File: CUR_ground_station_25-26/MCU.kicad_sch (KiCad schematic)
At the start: 1 part, among them U1 ESP32-S3-WROOM-1

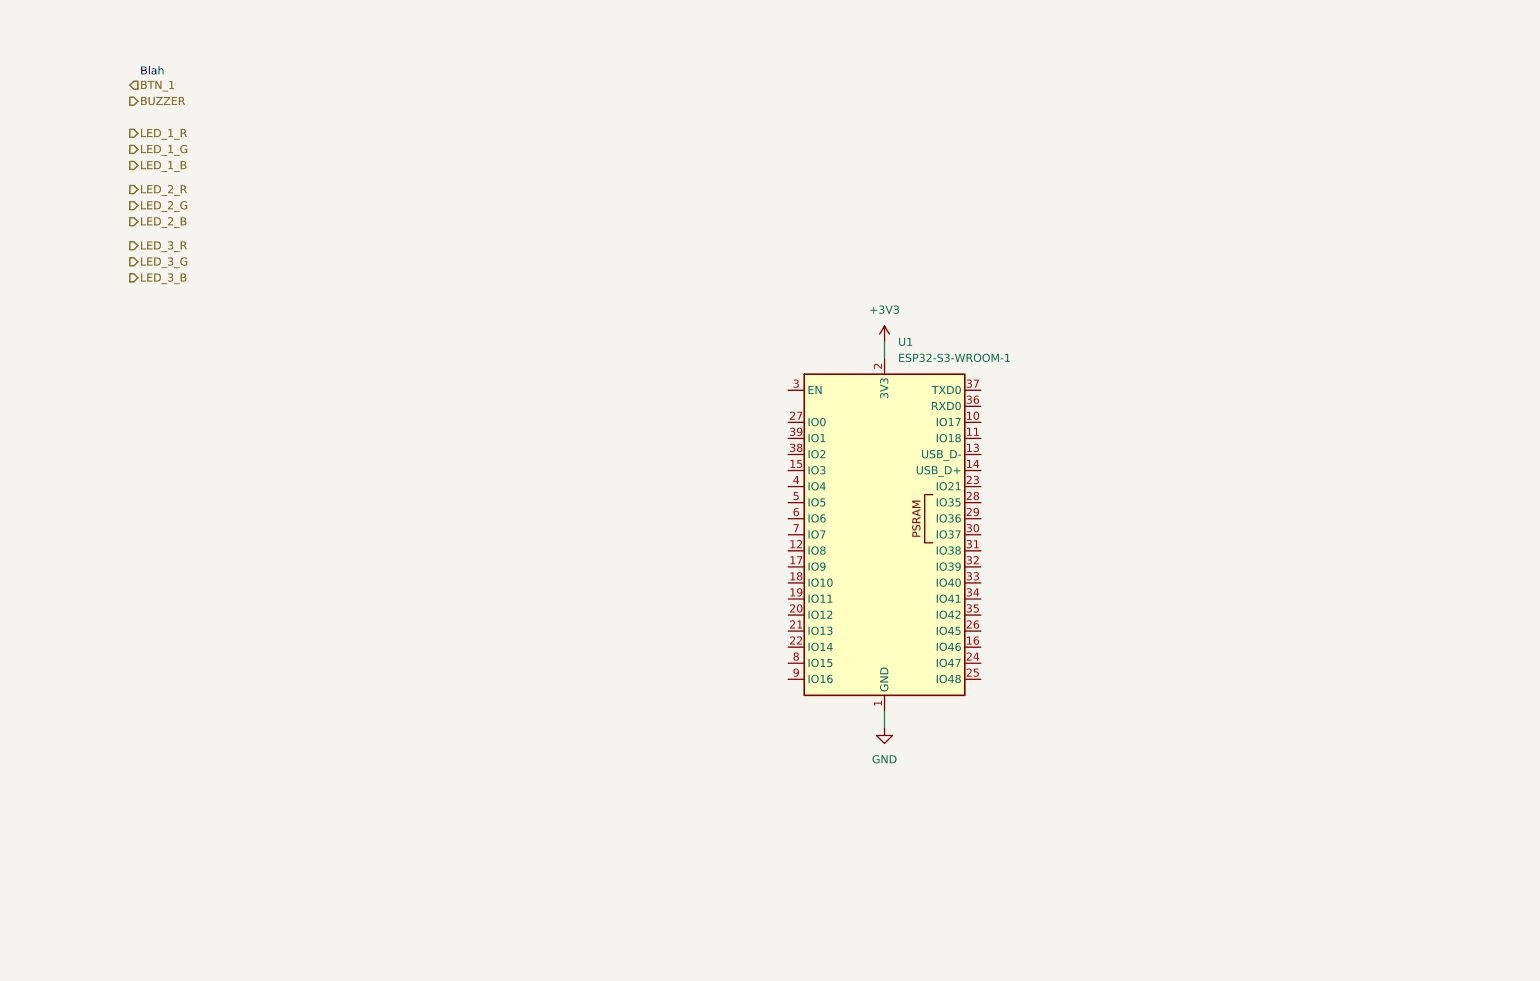
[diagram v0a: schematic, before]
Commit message: Add some required MCU components
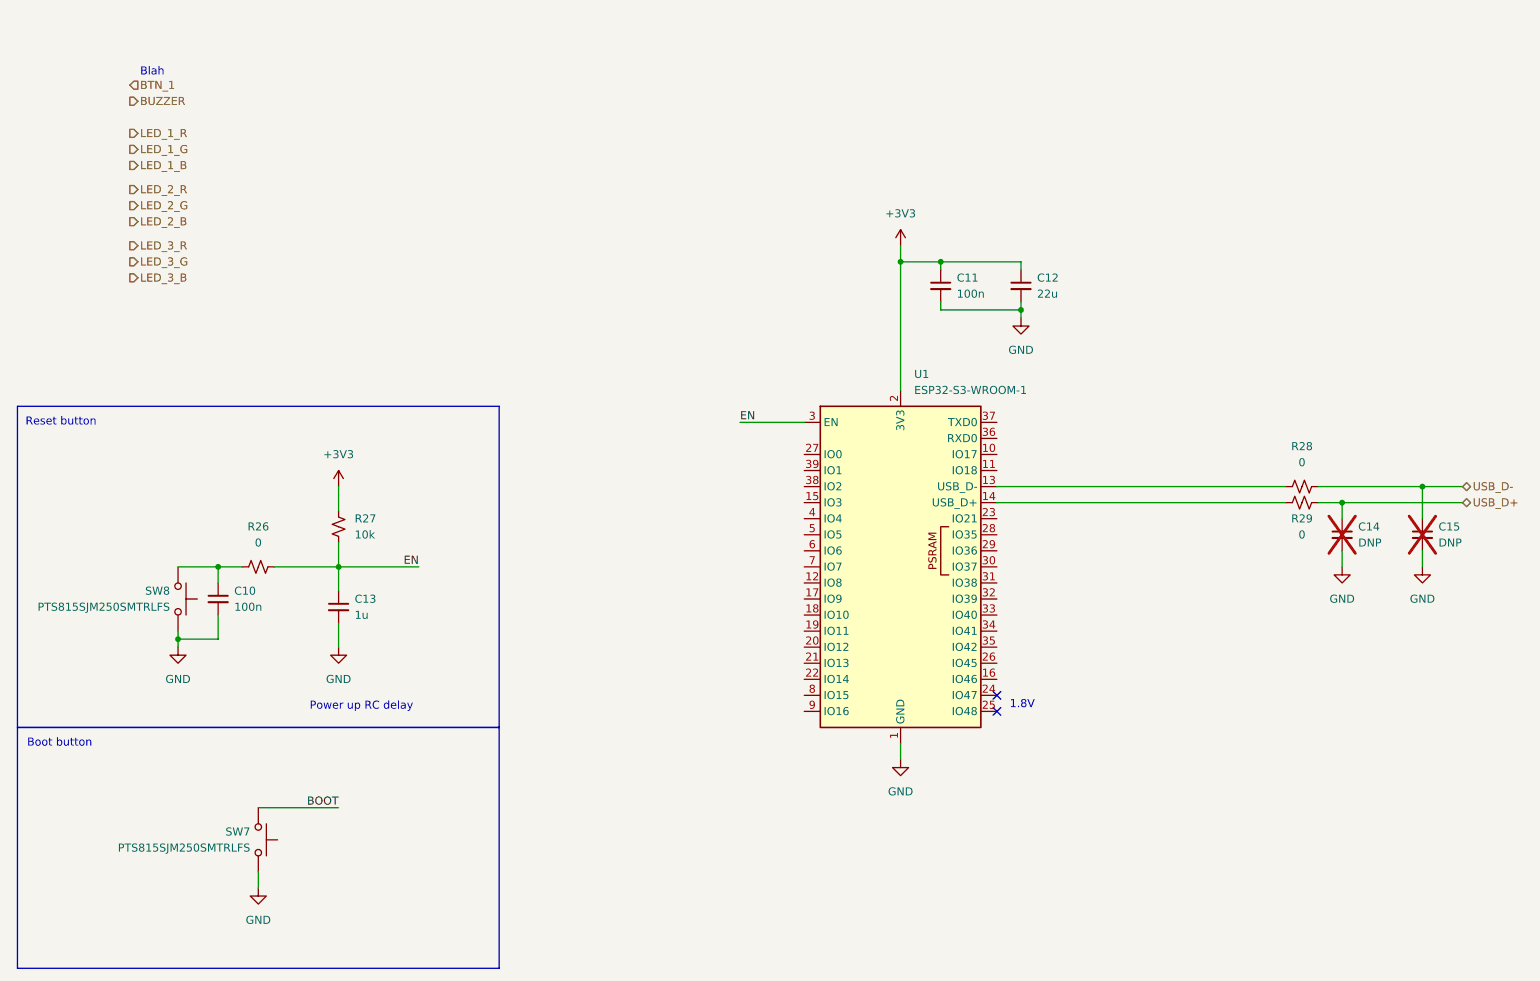
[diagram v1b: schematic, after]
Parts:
- added C10, C11: 100n, symbol Device:C_Small
- added C12: 22u, symbol Device:C_Small
- added C13: 1u, symbol Device:C_Small
- added C14, C15: DNP, symbol Device:C_Small
- added R26, R28, R29: 0, symbol Device:R_Small_US
- added R27: 10k, symbol Device:R_Small_US
- added SW7, SW8: PTS815SJM250SMTRLFS, symbol Switch:SW_Push
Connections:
- net +3V3: now also C11.1, C12.1, R27.1
- net GND: now also C10.2, C11.2, C12.2, C13.2, C14.2, C15.2, SW7.1, SW8.1
- net at U1.13 (USB_D-): now also R28.1
- net at U1.14 (USB_D+): now also R29.1
- net EN: now reaches U1.3 (EN)
- net EN: now also C13.1, R26.1, R27.2
- new net: C10.1, R26.2, SW8.2
- new net BOOT: SW7.2
- new net USB_D+: C14.1, R29.2
- new net USB_D-: C15.1, R28.2
- no-connect marks 0 -> 2
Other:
- note added: "1.8V"
- note added: "Boot button"
- note added: "Power up RC delay"
- note added: "Reset button"
- moved on the sheet: U1

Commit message: Sync sheet pins
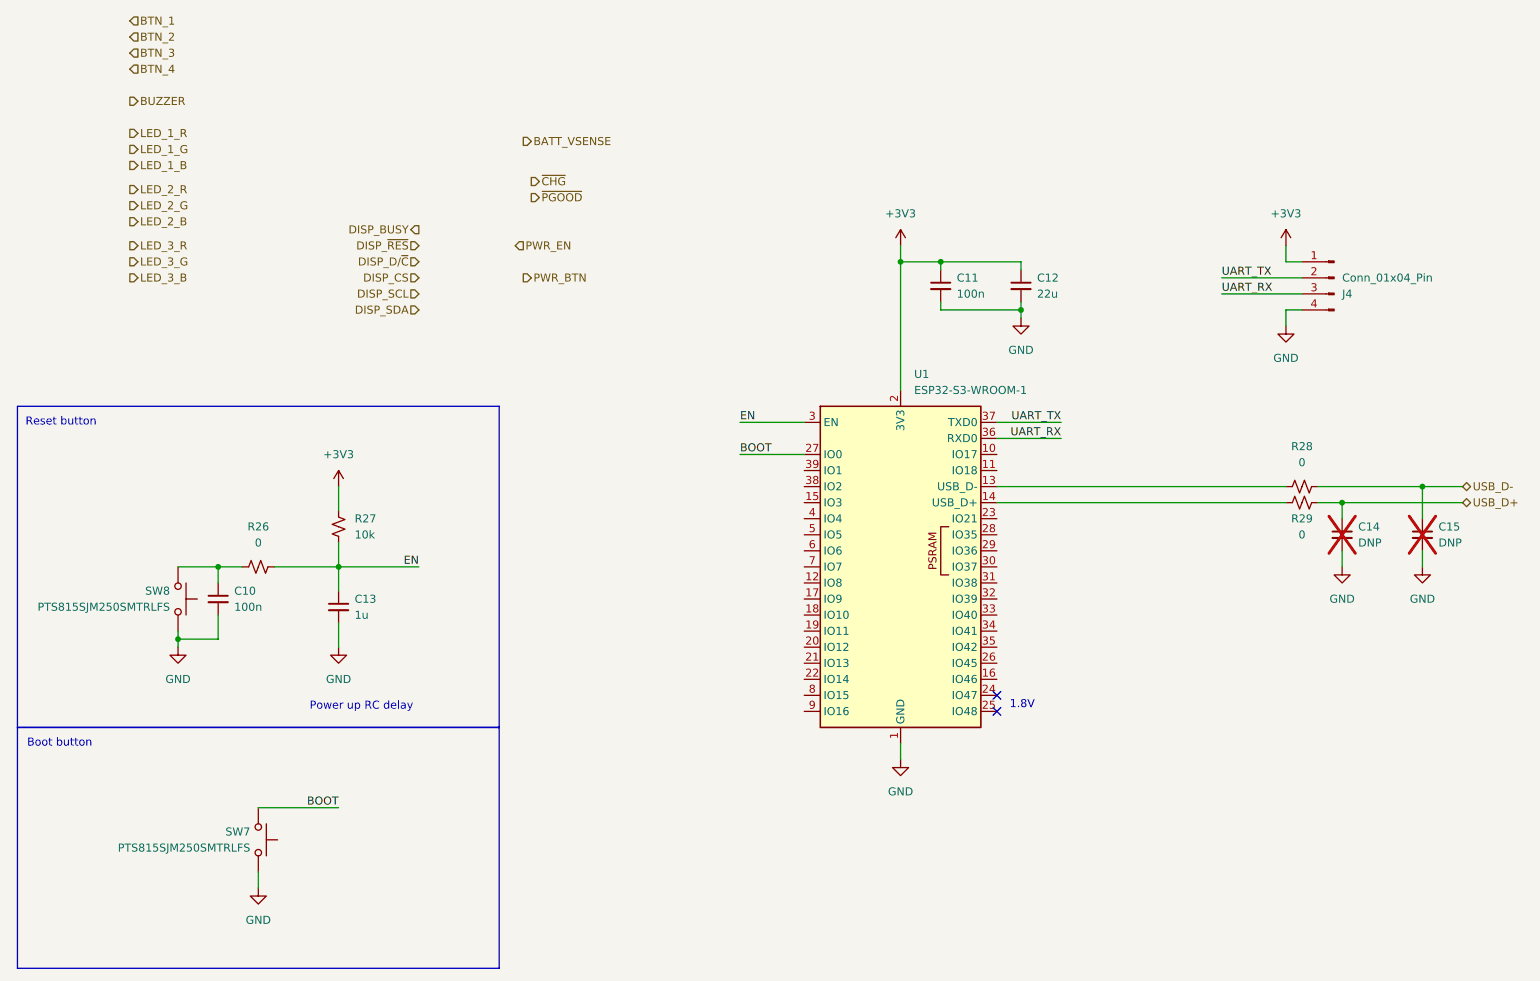
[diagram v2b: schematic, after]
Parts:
- added J4: Conn_01x04_Pin, symbol Connector:Conn_01x04_Pin
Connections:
- net +3V3: now also J4.1 (Pin_1)
- net BOOT: now also U1.27 (IO0)
- net GND: now also J4.4 (Pin_4)
- net UART_RX: now reaches U1.36 (RXD0)
- net UART_RX: now also J4.3 (Pin_3)
- net UART_TX: now reaches U1.37 (TXD0)
- net UART_TX: now also J4.2 (Pin_2)
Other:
- note removed: "Blah"

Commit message: Started placing pins on MCU
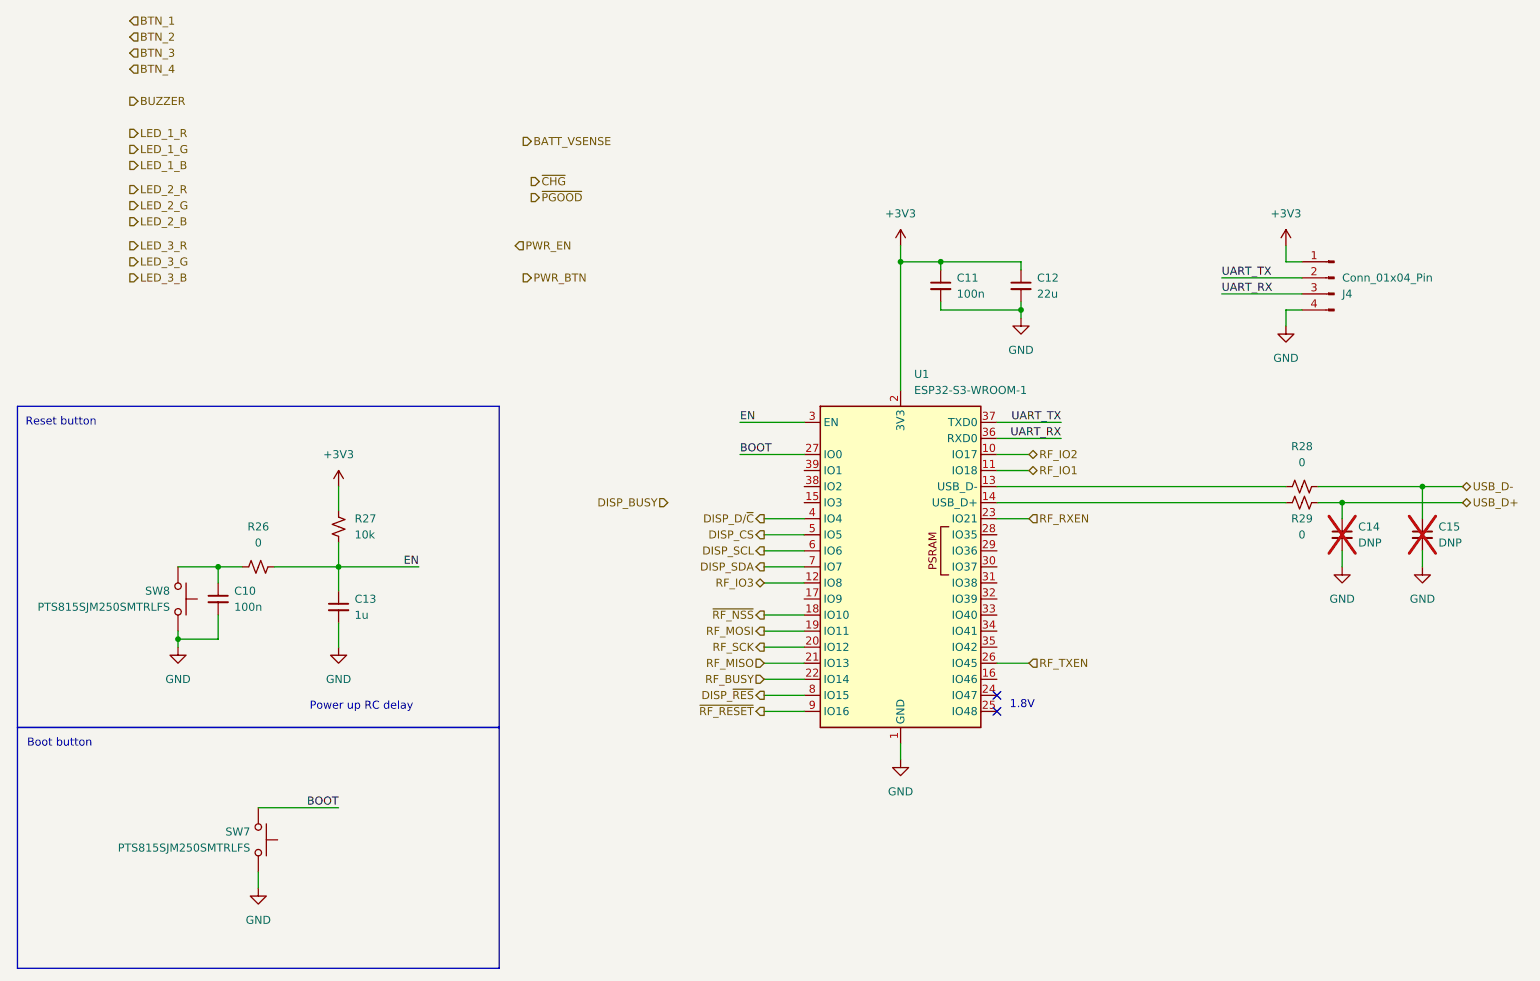
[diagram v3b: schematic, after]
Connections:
- net DISP_CS: now also U1.5 (IO5)
- net DISP_SCL: now also U1.6 (IO6)
- net DISP_SDA: now also U1.7 (IO7)
- net DISP_~{RES}: now also U1.8 (IO15)
- net RF_IO2: now reaches U1.10 (IO17)
- net RF_IO1: now reaches U1.11 (IO18)
- net RF_IO3: now reaches U1.12 (IO8)
- net ~{RF_NSS}: now reaches U1.18 (IO10)
- net RF_MOSI: now reaches U1.19 (IO11)
- net RF_SCK: now reaches U1.20 (IO12)
- net RF_MISO: now reaches U1.21 (IO13)
- net RF_BUSY: now reaches U1.22 (IO14)
- net RF_RXEN: now reaches U1.23 (IO21)
- net RF_TXEN: now reaches U1.26 (IO45)
- net DISP_D/~{C}: now reaches U1.4 (IO4)
- net ~{RF_RESET}: now reaches U1.9 (IO16)

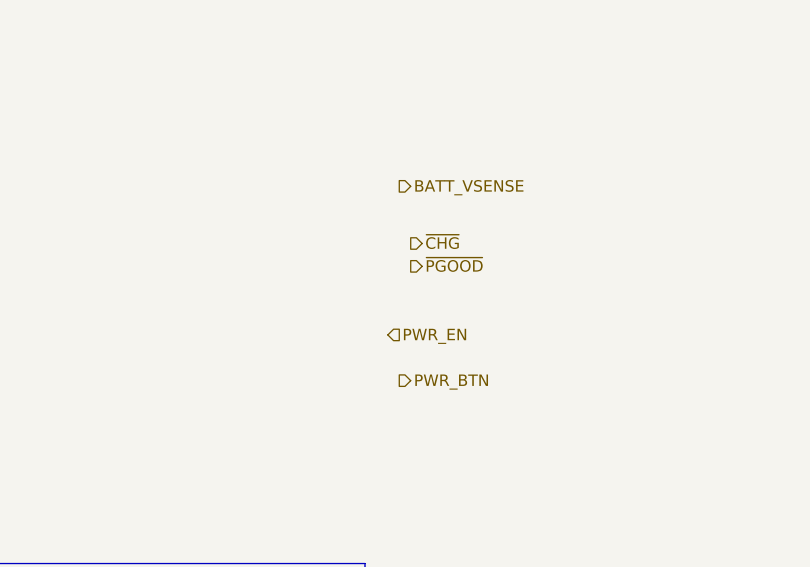
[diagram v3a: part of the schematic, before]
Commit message: sync sheet pins
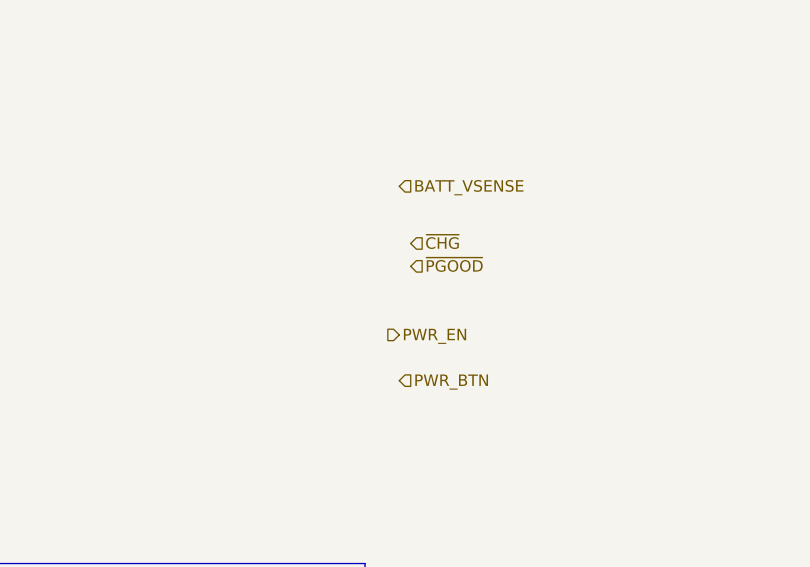
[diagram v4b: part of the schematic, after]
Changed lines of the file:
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@@
 	)
 	(hierarchical_label "PWR_BTN"
-		(shape output)
+		(shape input)
 		(at 92.71 55.88 0)
 		(effects
@@
 	)
 	(hierarchical_label "PWR_EN"
-		(shape input)
+		(shape output)
 		(at 91.44 50.8 0)
 		(effects
@@
 	)
 	(hierarchical_label "~{CHG}"
-		(shape output)
+		(shape input)
 		(at 93.98 40.64 0)
 		(effects
@@
 	)
 	(hierarchical_label "~{PGOOD}"
-		(shape output)
+		(shape input)
 		(at 93.98 43.18 0)
 		(effects
@@
 	)
 	(hierarchical_label "BATT_VSENSE"
-		(shape output)
+		(shape input)
 		(at 92.71 34.29 0)
 		(effects
